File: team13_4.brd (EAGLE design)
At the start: 28 x 47 mm, 39 parts, among them J1 FTDI_DEVICE, M1 WIRELESS-NRF24L01, U1 ATMEGA328P_TQFP, U2 GY-521MPU6050, U3 MAX1595EUA33+, Y1 8MHz

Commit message: Alleviated plane constrictions and stuff.
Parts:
- moved R1 2.69 mm to (9.15, 9.00)
- moved C6 2.00 mm to (10.9, 36.3)
- moved R8 2.00 mm to (19.7, 23.6)
- moved U2 2.00 mm to (14.2, 30.8)
- moved C5 2.00 mm to (8.50, 36.3)
- moved U$1 1.93 mm to (8.01, 7.99)
- moved Y1 1.24 mm to (13.6, 7.68)
- moved C3 1.00 mm to (11.7, 7.95)
- moved C12 0.80 mm to (12.0, 5.28), flipped to the top
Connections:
- net GND: now also U$1.3; no longer U$1.1
- net N$1: now also U$1.1; no longer U$1.3
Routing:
- net N$1: track 16.9 -> 10.0 mm, vias 2 -> 1
- net VIN: track 29.0 -> 25.9 mm
- net XTAL2: track 0.00 -> 2.58 mm
- net XTAL1: track 0.00 -> 2.56 mm
- net VCC: track 28.5 -> 26.1 mm, vias 4 -> 3
- net IMU_INT: track 15.5 -> 13.1 mm
- net NRF_SCK: track 35.1 -> 32.9 mm
- net AIN: track 17.6 -> 15.5 mm
- net GND: track 35.4 -> 33.7 mm, vias 9 -> 8
- net FTDI_RX: track 5.67 -> 4.14 mm, vias 1 -> 0
- net NRF_CE: track 40.3 -> 39.5 mm
- net IMU_SCL: track 22.6 -> 21.8 mm
- net NRF_CSN: track 34.7 -> 34.1 mm

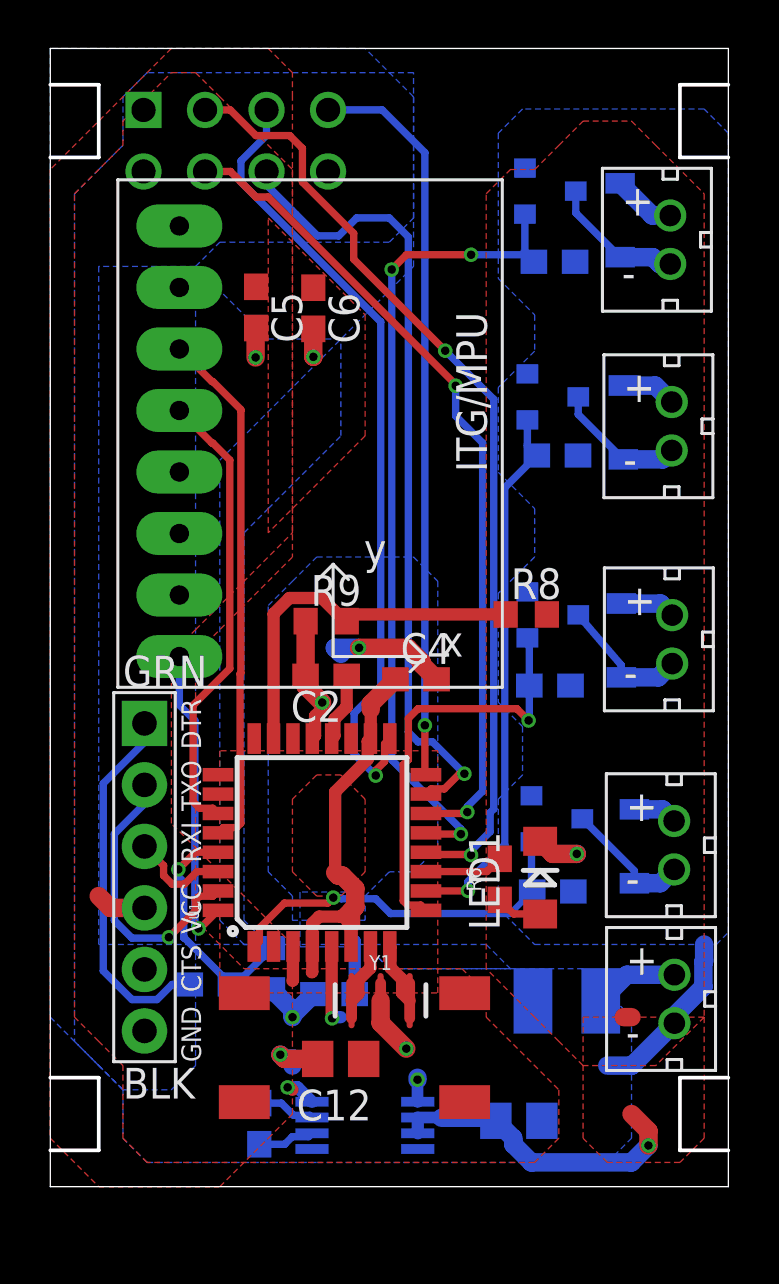
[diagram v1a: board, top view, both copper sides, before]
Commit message: fixed components on top of buttons
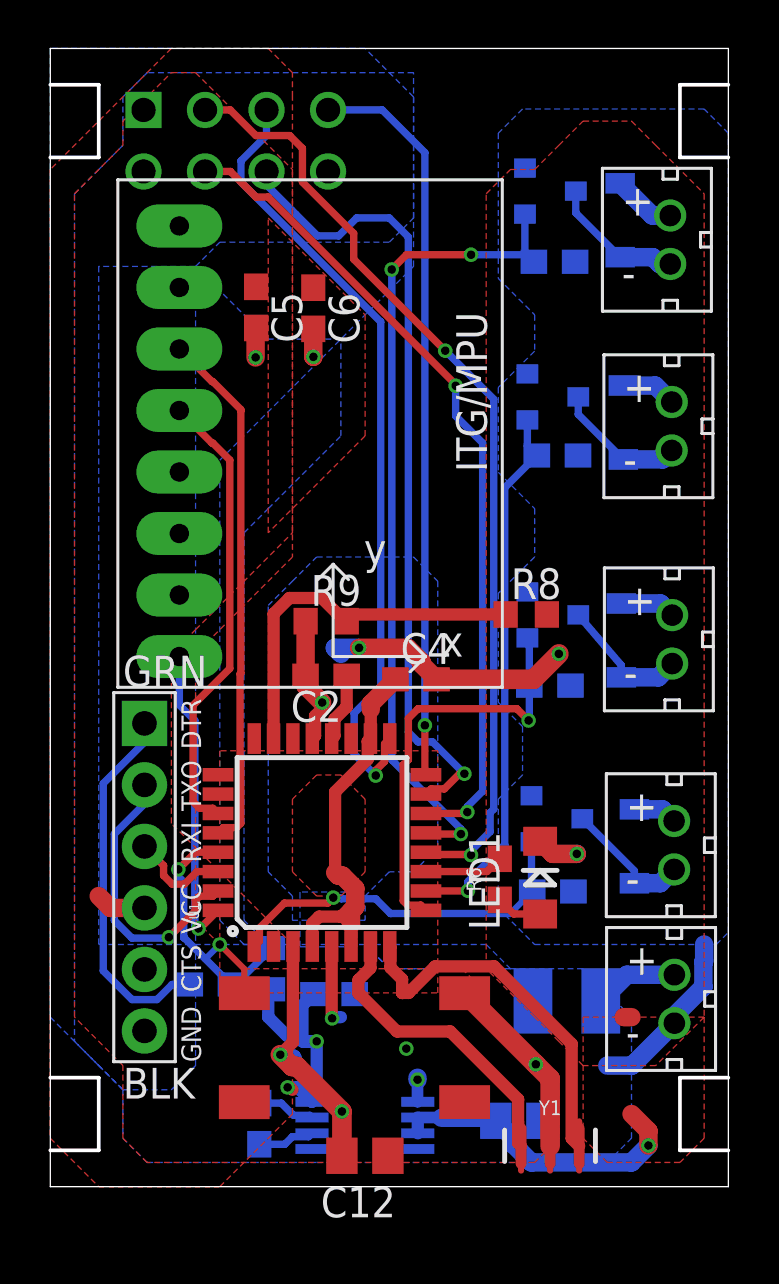
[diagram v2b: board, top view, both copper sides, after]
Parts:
- moved Y1 9.22 mm to (20.6, 1.68)
- moved C12 4.12 mm to (13.0, 1.28)
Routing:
- net GND: track 33.7 -> 49.4 mm, vias 8 -> 11
- net XTAL2: track 2.58 -> 15.3 mm
- net XTAL1: track 2.56 -> 12.5 mm
- net VCC: track 26.1 -> 31.7 mm
- net N$1: track 10.0 -> 13.3 mm, vias 1 -> 2
